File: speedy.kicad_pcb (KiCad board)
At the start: 2 copper layers, 0 parts

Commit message: Regenerate netlist & Start placing footprints
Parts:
- added A1: ANTENNA, _div:_ANT-2.45-CHP, F.Cu at (148.5, 93.0)
- added C1: 4.7uF, _std:_0402, F.Cu at (229.2, 82.7)
- added C10: 10pF, _std:_0402, F.Cu at (203.1, 79.5)
- added C11: 10pF, _std:_0402, F.Cu at (229.1, 76.6)
- added C12: 10uF, _std:_0603, F.Cu at (201.3, 84.5)
- added C13: 0.1uF, _std:_0402, F.Cu at (232.3, 69.4)
- added C15: 0.1uF, _std:_0402, F.Cu at (257.3, 73.6)
- added C16: 10nF, _std:_0402, F.Cu at (254.9, 73.6)
- added C17: 0.1uF, _std:_0402, F.Cu at (261.4, 71.7)
- added C18: 0.1uF, _std:_0402, F.Cu at (255.0, 76.6)
- added C19: 0.1uF, _std:_0402, F.Cu at (259.8, 74.7)
- added C2: 0.1uF, _std:_0402, F.Cu at (221.8, 85.8)
- added C20: 4.7uF, _std:_0402, F.Cu at (263.9, 71.7)
- added C21: 0.1uF, _std:_0402, F.Cu at (267.2, 49.4)
- added C22: 22pF, _std:_0402, F.Cu at (264.8, 49.4)
- added C23: 33nF, _std:_0402, F.Cu at (267.8, 46.4)
- added C24: 10nF, _std:_0402, F.Cu at (265.5, 43.3)
- added C25: 1nF, _std:_0402, F.Cu at (248.0, 47.9)
- added C26: 22pF, _std:_0402, F.Cu at (262.9, 46.4)
- added C27: 2.2nF, _std:_0402, F.Cu at (263.1, 43.3)
- added C28: 4.7pF, _std:_0402, F.Cu at (260.5, 46.4)
- added C29: 1.5pF, _std:_0402, F.Cu at (262.4, 49.4)
- added C3: 0.1uF, _std:_0402, F.Cu at (232.3, 66.4)
- added C30: 1pF, _std:_0402, F.Cu at (260.2, 49.4)
- added C31: 0.1uF, _std:_0402, F.Cu at (217.8, 55.2)
- added C32: 0.1uF, _std:_0402, F.Cu at (226.0, 48.0)
- added C33: 100uF, _std:_0402, F.Cu at (214.2, 58.3)
- added C34: 100uF, _std:_0402, F.Cu at (211.5, 58.3)
- added C35: 10uF, _std:_0603, F.Cu at (211.4, 60.4)
- added C36: 10uF, _std:_0603, F.Cu at (207.0, 40.4)
- added C37: 0.1uF, _std:_0402, F.Cu at (230.6, 46.6)
- added C38: 10uF, _std:_0603, F.Cu at (203.0, 60.8)
- added C39: 10uF, _std:_0603, F.Cu at (213.9, 60.4)
- added C4: 0.1uF, _std:_0402, F.Cu at (232.3, 72.5)
- added C40: 4.7uF, _std:_0402, F.Cu at (220.3, 55.2)
- added C41: 0.1uF, _std:_0402, F.Cu at (226.6, 57.0)
- added C42: 4.7uF, _std:_0402, F.Cu at (226.6, 54.0)
- added C43: 0.1uF, _std:_0402, F.Cu at (235.5, 46.4)
- added C44: 0.1uF, _std:_0402, F.Cu at (233.1, 49.4)
- added C45: 10uF, _std:_0603, F.Cu at (216.4, 60.4)
- added C46: 10uF, _std:_0603, F.Cu at (219.4, 60.3)
- added C5: 1uF, _std:_0402, F.Cu at (205.1, 79.5)
- added C6: 0.1uF, _std:_0402, F.Cu at (226.7, 76.6)
- added C7: 2.2uF, _std:_0402, F.Cu at (216.0, 87.5)
- added C8: 2.2uF, _std:_0402, F.Cu at (218.5, 87.5)
- added C9: 0.1uF, _std:_0402, F.Cu at (217.6, 80.7)
- added CONN1: JTAG, _connectors:_Molex-PicoBlade-SMD-8, F.Cu at (148.6, 116.7)
- added CONN10: MOTOR_3, _connectors:_Solder_Pad1.27_2, F.Cu at (166.2, 122.8)
- added CONN11: MOTOR_4, _connectors:_Solder_Pad1.27_2, F.Cu at (130.7, 122.8)
- added CONN3: MICRO_SD, _div:_Molex-microSD-WM6701, F.Cu at (136.7, 105.0)
- added CONN4: MICRO_USB, _connectors:_Micro-USB-AB-receptacle-SMT, B.Cu at (148.6, 113.9)
- added CONN7: PWR, _connectors:_Pin2mm_2, F.Cu at (160.3, 104.8)
- added CONN8: MOTOR_1, _connectors:_Solder_Pad1.27_2, F.Cu at (130.7, 87.2)
- added CONN9: MOTOR_2, _connectors:_Solder_Pad1.27_2, F.Cu at (166.2, 87.2)
- added D1: POWER, _std:_LED_0603, F.Cu at (228.2, 72.5)
- added D10: APT1608F3C, _std:_LED_0603, F.Cu at (205.5, 44.4)
- added D11: APT1608F3C, _std:_LED_0603, F.Cu at (194.6, 54.6)
- added D12: APT1608F3C, _std:_LED_0603, F.Cu at (216.6, 37.2)
- added D13: APT1608F3C, _std:_LED_0603, F.Cu at (204.4, 49.5)
- added D14: APT1608F3C, _std:_LED_0603, F.Cu at (215.3, 42.3)
- added D15: APT1608F3C, _std:_LED_0603, F.Cu at (226.4, 37.2)
- added D16: APT1608F3C, _std:_LED_0603, F.Cu at (204.4, 54.6)
- added D2: ERROR, _std:_LED_0603, F.Cu at (223.3, 81.7)
- added D3: STATUS, _std:_LED_0603, F.Cu at (228.0, 67.4)
- added D4: HEARTBEAT, _std:_LED_0603, F.Cu at (210.4, 85.2)
- added D5: SBR130S3-7, _std:_SOD-323, F.Cu at (208.8, 89.0)
- added D8: CHARGE_LED, _std:_LED_0603, F.Cu at (206.8, 37.2)
- added D9: APT1608F3C, _std:_LED_0603, F.Cu at (194.6, 49.5)
- added F1: 500mA, _std:_0402, F.Cu at (227.5, 79.6)
- added F2: Fuse 3A, _std:_0402, F.Cu at (203.4, 58.7)
- added L1: 8.2nH, _std:_0402, F.Cu at (260.6, 43.3)
- added L2: 3.9nH, _std:_0402, F.Cu at (268.0, 43.3)
- added L3: 2.7nH, _std:_0402, F.Cu at (265.4, 46.4)
- added Q2: 2N7002, _std:_SOT23-3, F.Cu at (198.9, 60.4)
- added Q3: 2N7002, _std:_SOT23-3, F.Cu at (195.1, 60.4)
- added R1: 100k, _std:_0402, F.Cu at (229.9, 87.5)
- added R11: 1k, _std:_0402, F.Cu at (231.9, 78.5)
- added R12: 1k, _std:_0402, F.Cu at (224.0, 85.8)
- added R13: 1k, _std:_0402, F.Cu at (227.0, 82.7)
- added R14: 1k, _std:_0402, F.Cu at (230.0, 79.6)
- added R15: 47k, _std:_0402, F.Cu at (257.2, 76.6)
- added R16: 47k, _std:_0402, F.Cu at (259.1, 77.7)
- added R17: 1M, _std:_0402, F.Cu at (269.9, 46.4)
- added R18: 22k, _std:_0402, F.Cu at (269.4, 49.4)
- added R19: 10m, _std:_0402, F.Cu at (217.6, 51.6)
- added R2: 10k, _std:_0402, F.Cu at (227.9, 88.7)
- added R20: 10k, _std:_0402, F.Cu at (228.3, 44.5)
- added R21: 10k, _std:_0402, F.Cu at (228.3, 47.5)
- added R22: 3.3k, _std:_0402, F.Cu at (219.2, 58.2)
- added R23: 2.05k, _std:_0402, F.Cu at (221.4, 58.2)
- added R24: 3.3k, _std:_0402, F.Cu at (225.8, 51.0)
- added R25: 2.05k, _std:_0402, F.Cu at (216.9, 58.3)
- added R26: 2.8k, _std:_0402, F.Cu at (227.8, 51.0)
- added R27: 2k, _std:_0402, F.Cu at (233.3, 46.4)
- added R28: 330, _std:_0402, F.Cu at (235.2, 43.4)
- added R29: 2k, _std:_0402, F.Cu at (224.4, 55.2)
- added R3: 10k, _std:_0402, F.Cu at (231.4, 84.5)
- added R30: 10k, _std:_0402, F.Cu at (230.2, 49.6)
- added R31: 100, _std:_0402, F.Cu at (222.5, 55.2)
- added R32: 40, _std:_0402, F.Cu at (233.3, 43.4)
- added R33: 10k, _std:_0402, F.Cu at (237.1, 43.4)
- added R34: 100, _std:_0402, F.Cu at (223.6, 58.2)
- added R35: 40, _std:_0402, F.Cu at (229.8, 52.6)
- added R4: 10k, _std:_0402, F.Cu at (227.9, 85.7)
- added R5: 10k, _std:_0402, F.Cu at (233.7, 78.5)
- added R6: 4.7k, _std:_0402, F.Cu at (231.9, 81.5)
- added R7: 10k, _std:_0402, F.Cu at (233.7, 75.5)
- added R8: 4.7k, _std:_0402, F.Cu at (226.0, 85.8)
- added R9: 10k, _std:_0402, F.Cu at (231.9, 75.5)
- added SW1: Pushbutton, _div:_PTS525SK15-SMT-Pushbutton, F.Cu at (214.6, 47.3)
- added U1: STM32F415RGT6, _lqfp:_LQFP64, F.Cu at (145.2, 109.6)
- added U10: LT1965, Housings_DFN_QFN:DFN-8-1EP_3x3mm_Pitch0.5mm, B.Cu at (156.3, 107.1)
- added U11: INA213-SC70, _std:SC70, F.Cu at (195.2, 44.3)
- added U12: MCP73831, _std:_TSOT23-5, F.Cu at (190.9, 60.5)
- added U13: DRV8839, _div:TI-DRV8839_PWSON-N12, B.Cu at (134.2, 90.8)
- added U14: DRV8839, _div:TI-DRV8839_PWSON-N12, B.Cu at (134.4, 119.1)
- added U2: NUF2042VX6, _std:SOT-563_6-lead, B.Cu at (148.9, 111.5)
- added U4: MPU-9250, Housings_DFN_QFN:QFN-24-1EP_3x3mm_Pitch0.4mm, B.Cu at (149.1, 99.3)
- added U5: MS5611-01BA, _sensors:_MS5611-01BA, F.Cu at (263.1, 67.7)
- added U6: VL6180X, _sensors:VL6180X, B.Cu at (149.1, 104.5)
- added U7: NRF24L01+, Housings_DFN_QFN:QFN-20-1EP_4x4mm_Pitch0.5mm, B.Cu at (155.1, 94.9)
- added U8: LTC2955DDB-1, Housings_DFN_QFN:DFN-10-1EP_2x3mm_Pitch0.5mm, B.Cu at (158.8, 112.0)
- added U9: LT1965, Housings_DFN_QFN:DFN-8-1EP_3x3mm_Pitch0.5mm, B.Cu at (156.3, 102.4)
- added X1: 16Mhz 10ppm, _div:_TSX-3225-SMD-XTAL, B.Cu at (144.3, 109.5)
- added X2: 16MHz 10ppm, _div:_TSX-3225-SMD-XTAL, B.Cu at (159.8, 94.7)

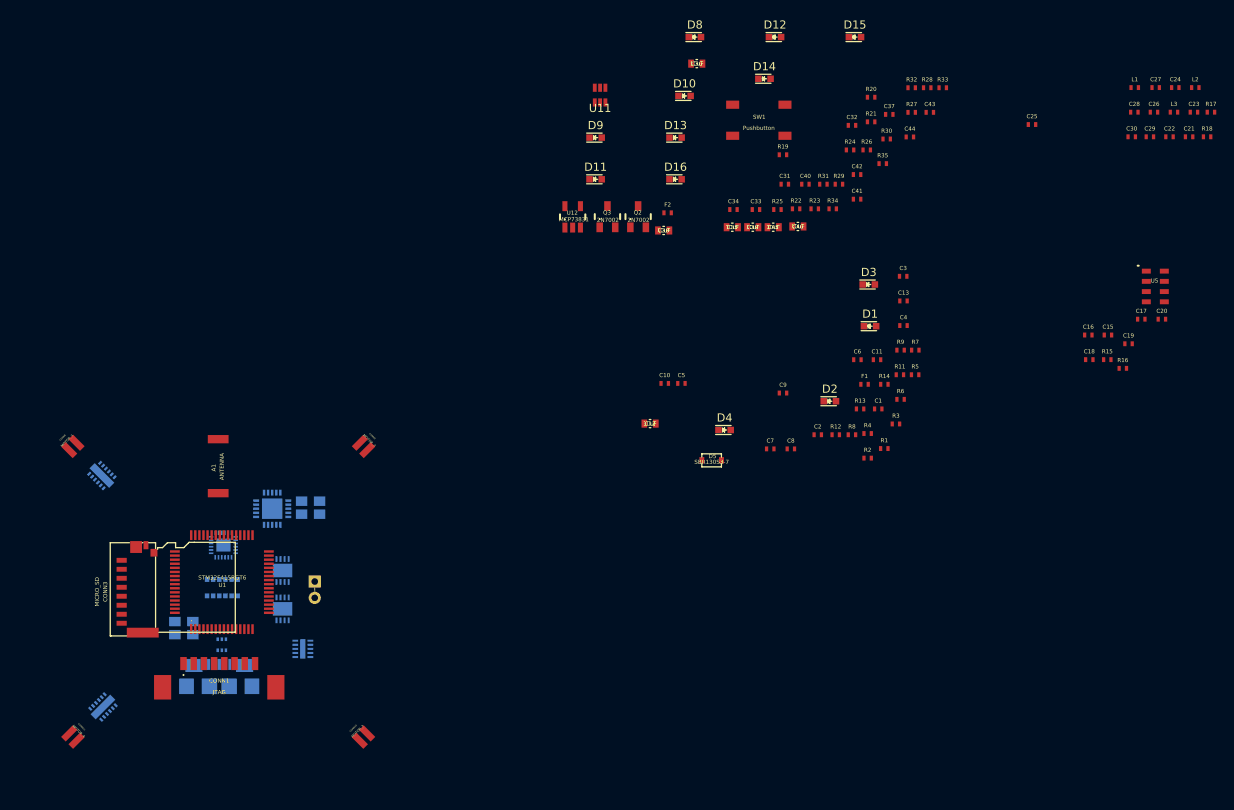
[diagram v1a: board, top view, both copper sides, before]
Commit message: Finish placing components on PCB
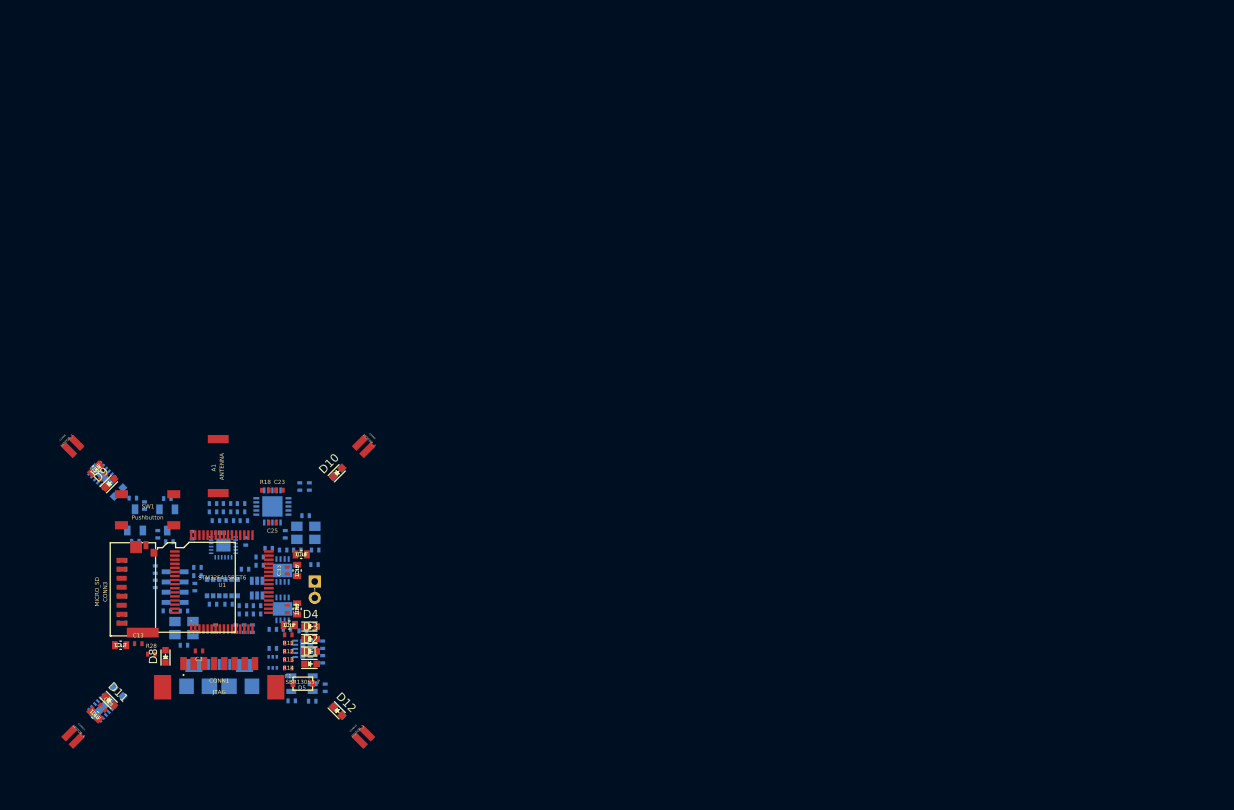
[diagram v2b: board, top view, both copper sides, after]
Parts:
- removed R2: 10k, _std:_0402
- C1, C10, C11, C15, C16, C17, C18, C19, C2, C20, C21, C22, C24, C26, C27, C28, C29, C30, C31, C32, C37, C4, C40, C41, C42, C5, C6, C7, C8, C9, D13, D14, D15, D16, F2, L1, L2, L3, Q2, Q3, R1, R15, R16, R17, R19, R20, R21, R22, R23, R24, R25, R26, R27, R29, R3, R30, R31, R32, R33, R34, R35, R4, R5, R6, R7, R8, R9, U11, U12, U5: moved to B.Cu
- moved L2 128.9 mm to (149.5, 94.2), turned to 180 degrees
- moved U5 125.4 mm to (143.2, 104.5), turned to 180 degrees
- moved R17 124.5 mm to (156.7, 98.0), turned to 90 degrees
- moved L3 124.2 mm to (151.3, 95.2), turned to 180 degrees
- moved C27 123.5 mm to (151.6, 96.3), turned to 180 degrees
- moved C29 123.1 mm to (147.8, 94.2), turned to 180 degrees
- moved R18 123.1 mm to (154.2, 92.6)
- moved C30 121.4 mm to (147.8, 95.2)
- moved C28 121.3 mm to (149.5, 95.2), turned to 180 degrees
- moved C23 121.1 mm to (156.0, 92.6)
- moved C44 120.9 mm to (134.3, 119.2), turned to 315 degrees
- moved L1 120.6 mm to (151.3, 94.2)
- moved D15 120.6 mm to (136.3, 117.3), turned to 135 degrees
- moved C20 119.4 mm to (149.7, 106.6), turned to 180 degrees
- moved C24 117.7 mm to (158.4, 92.2), turned to 270 degrees
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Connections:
- U1 pad 28: /Power/MOTOR_3_EN -> GND
- U1 pad 4: Net-(U1-Pad4) -> /Power/MOTOR_3_EN
- U1 pad 60: Net-(R2-Pad1) -> VCC

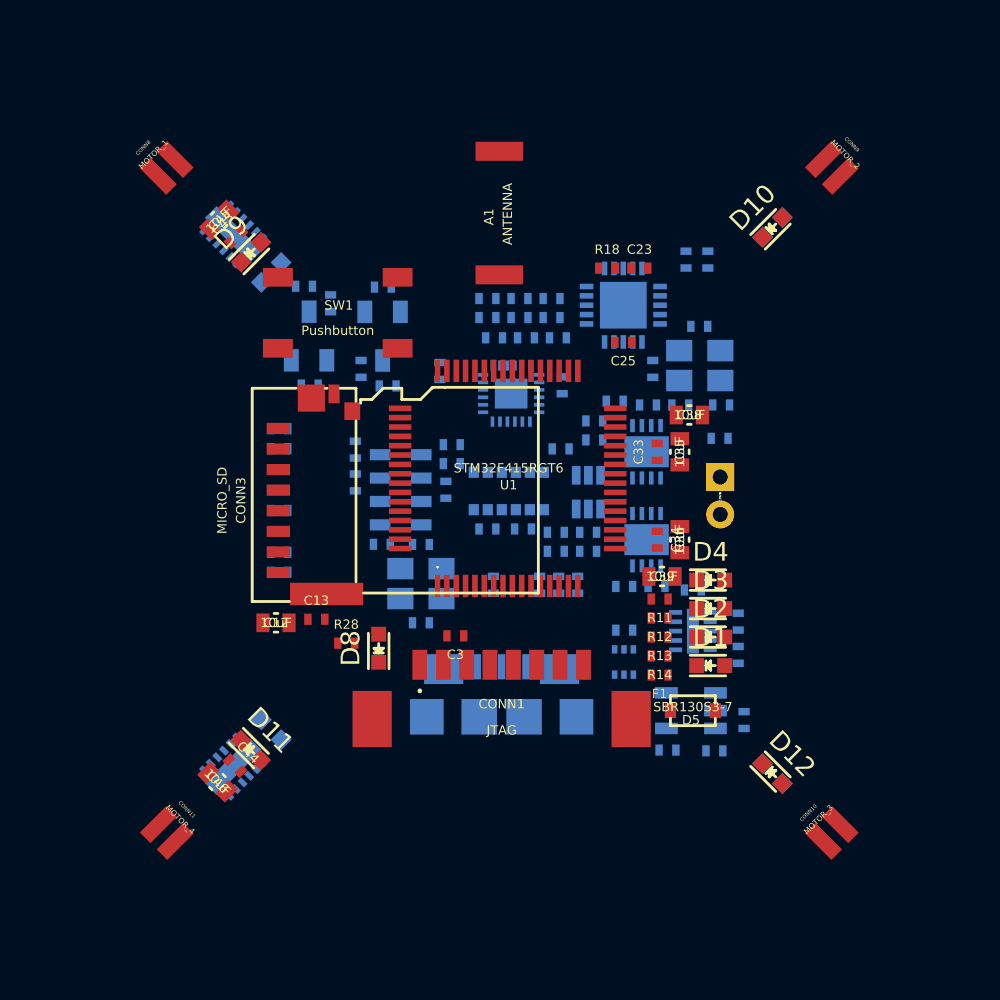
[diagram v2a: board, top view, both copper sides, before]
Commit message: Draw edge cuts
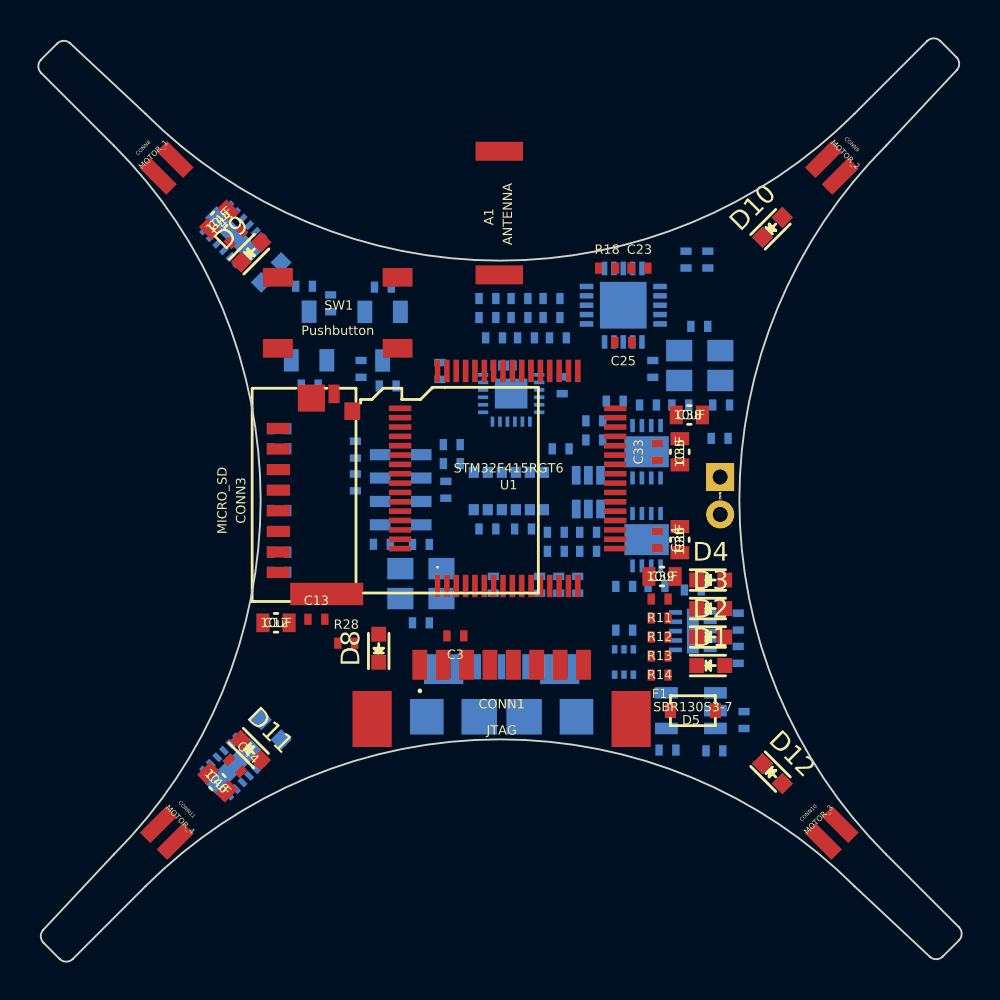
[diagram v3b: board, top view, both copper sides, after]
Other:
- board outline added: 49.4 x 49.4 mm
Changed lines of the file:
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@@
     (links 335)
     (no_connects 335)
-    (area 0 0 0 0)
+    (area 108.853119 65.355619 188.149081 144.651581)
     (thickness 1.6)
-    (drawings 24)
+    (drawings 48)
     (tracks 0)
     (zones 0)
@@
   (gr_line (start 173.036634 128.550255) (end 172.175154 129.409131) (layer Dwgs.User) (width 0.1))
   (gr_line (start 169.148618 123.954062) (end 173.03717 127.842613) (layer Dwgs.User) (width 0.1))
+  (gr_arc (start 172.552543 81.682564) (end 172.917679 82.024143) (angle -88.0041125) (layer Edge.Cuts) (width 0.1))
+  (gr_arc (start 171.693667 80.821084) (end 172.047755 80.468066) (angle -90.08673507) (layer Edge.Cuts) (width 0.1))
+  (gr_arc (start 148.5011 65.40562) (end 129.550638 84.356082) (angle -90) (layer Edge.Cuts) (width 0.1))
+  (gr_arc (start 125.180064 80.952157) (end 125.521643 80.587021) (angle -88.0041125) (layer Edge.Cuts) (width 0.1))
+  (gr_arc (start 124.318584 81.811033) (end 123.965566 81.456945) (angle -90.08673507) (layer Edge.Cuts) (width 0.1))
+  (gr_arc (start 108.90312 105.0036) (end 127.853582 123.954062) (angle -90) (layer Edge.Cuts) (width 0.1))
+  (gr_arc (start 124.449657 128.324636) (end 124.084521 127.983057) (angle -88.0041125) (layer Edge.Cuts) (width 0.1))
+  (gr_arc (start 125.308533 129.186116) (end 124.954445 129.539134) (angle -90.08673507) (layer Edge.Cuts) (width 0.1))
+  (gr_arc (start 148.5011 144.60158) (end 167.451562 125.651118) (angle -90) (layer Edge.Cuts) (width 0.1))
+  (gr_arc (start 171.822136 129.055043) (end 171.480557 129.420179) (angle -88.0041125) (layer Edge.Cuts) (width 0.1))
+  (gr_arc (start 172.683616 128.196167) (end 173.036634 128.550255) (angle -90.08673507) (layer Edge.Cuts) (width 0.1))
+  (gr_arc (start 188.09908 105.0036) (end 169.148618 86.053138) (angle -90) (layer Edge.Cuts) (width 0.1))
+  (gr_line (start 172.917679 82.024143) (end 169.148618 86.053138) (layer Edge.Cuts) (width 0.1))
+  (gr_line (start 172.047755 80.468066) (end 172.906631 81.329546) (layer Edge.Cuts) (width 0.1))
+  (gr_line (start 167.451562 84.356082) (end 171.340113 80.46753) (layer Edge.Cuts) (width 0.1))
+  (gr_line (start 125.521643 80.587021) (end 129.550638 84.356082) (layer Edge.Cuts) (width 0.1))
+  (gr_line (start 123.965566 81.456945) (end 124.827046 80.598069) (layer Edge.Cuts) (width 0.1))
+  (gr_line (start 127.853582 86.053138) (end 123.96503 82.164587) (layer Edge.Cuts) (width 0.1))
+  (gr_line (start 124.084521 127.983057) (end 127.853582 123.954062) (layer Edge.Cuts) (width 0.1))
+  (gr_line (start 124.954445 129.539134) (end 124.095569 128.677654) (layer Edge.Cuts) (width 0.1))
+  (gr_line (start 129.550638 125.651118) (end 125.662087 129.53967) (layer Edge.Cuts) (width 0.1))
+  (gr_line (start 171.480557 129.420179) (end 167.451562 125.651118) (layer Edge.Cuts) (width 0.1))
+  (gr_line (start 173.036634 128.550255) (end 172.175154 129.409131) (layer Edge.Cuts) (width 0.1))
+  (gr_line (start 169.148618 123.954062) (end 173.03717 127.842613) (layer Edge.Cuts) (width 0.1))
 )

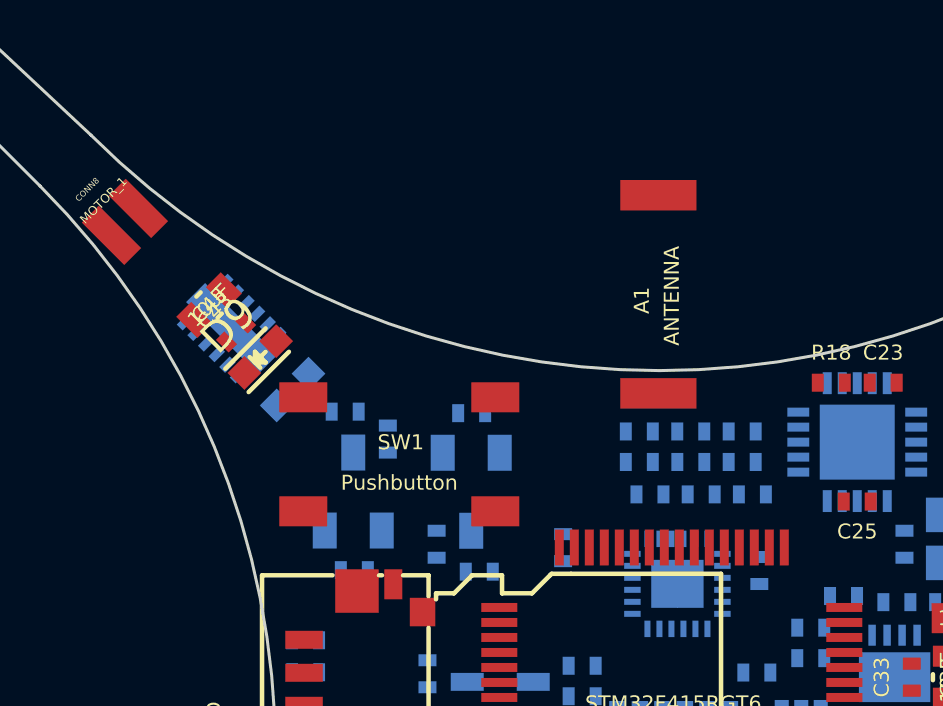
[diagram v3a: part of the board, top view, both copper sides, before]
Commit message: Change pushbutton for a radially mounted button
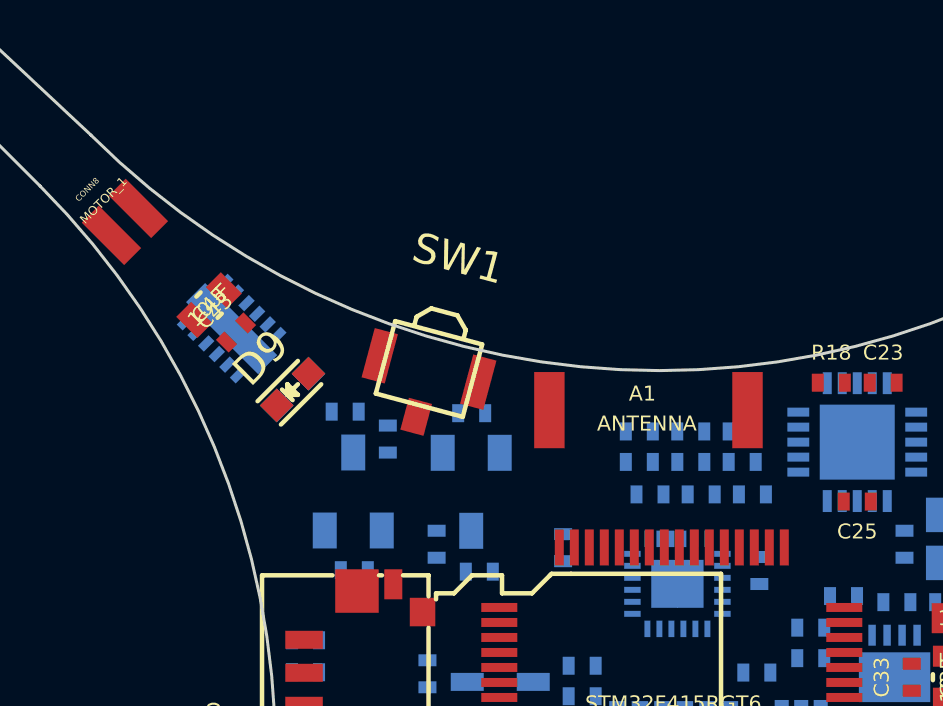
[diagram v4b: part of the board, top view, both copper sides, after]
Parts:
- SW1: value Pushbutton -> PushButton; footprint _div:_PTS525SK15-SMT-Pushbutton -> _div:SMD_Pushbutton_B3U-3100P
- moved A1 3.67 mm to (144.8, 93.5), turned to 0 degrees
- moved SW1 3.01 mm to (140.8, 92.2), turned to 345 degrees
- moved D9 1.53 mm to (136.3, 92.8)
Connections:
- SW1 pad 1: GND -> Net-(SW1-Pad1)
- SW1 pad 2: Net-(SW1-Pad2) -> GND
- U8 pad 5: Net-(SW1-Pad2) -> Net-(SW1-Pad1)

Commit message: Change micro USB connector & add 3d models to some footprints
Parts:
- CONN4: footprint _connectors:_Micro-USB-AB-receptacle-SMT -> _connectors:_Micro-USB-AB-receptacle-SMT-th
- moved R29 7.28 mm to (153.5, 115.0), turned to 270 degrees
- moved C40 4.20 mm to (153.5, 116.9), turned to 90 degrees
- moved D10 3.36 mm to (160.7, 92.8), turned to 315 degrees
- moved D14 3.36 mm to (160.7, 92.8), turned to 135 degrees
- moved D16 3.30 mm to (160.7, 117.3), turned to 45 degrees
- moved D12 3.30 mm to (160.7, 117.3), turned to 45 degrees
- moved CONN4 2.68 mm to (148.5, 116.6)
- moved C42 2.23 mm to (159.8, 115.4)
- moved U12 1.91 mm to (158.1, 115.1)
- moved R28 1.57 mm to (138.7, 112.7)
- moved D11 1.55 mm to (136.3, 117.3), turned to 135 degrees
- moved C21 1.53 mm to (158.6, 93.3), turned to 0 degrees
- moved D8 1.15 mm to (140.9, 112.9)
- moved D5 0.98 mm to (158.0, 116.8), turned to 270 degrees
- moved C24 0.88 mm to (158.6, 91.3), turned to 0 degrees
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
